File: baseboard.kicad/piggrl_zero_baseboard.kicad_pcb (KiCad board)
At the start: 2 copper layers, 101 x 43.9 mm, 61 parts, among them P1 PowerBoost 500c, P2 I2C, P3 USB_A, P4 Serial, Q1 IRF7309IPBF, Q4 MMBT2222, SW1 SW_PUSH, U1 gpio-header_zero, U2 2.2_tft_ili9340, U3 Regulator_LP2980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

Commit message: added more 3d models
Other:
- board text added: "2016-03-13"
- board text removed: "2016-03-05"

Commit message: added a nice 8bit-ish logo to the front silkscreen :-)
... that will be covered by the screen :'-(
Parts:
- added G***: LOGO, components:Logo, F.Cu at (167.5, 133.1)
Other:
- board text added: "Gnd Tx Rx"
- board text removed: "RX TX Gnd"

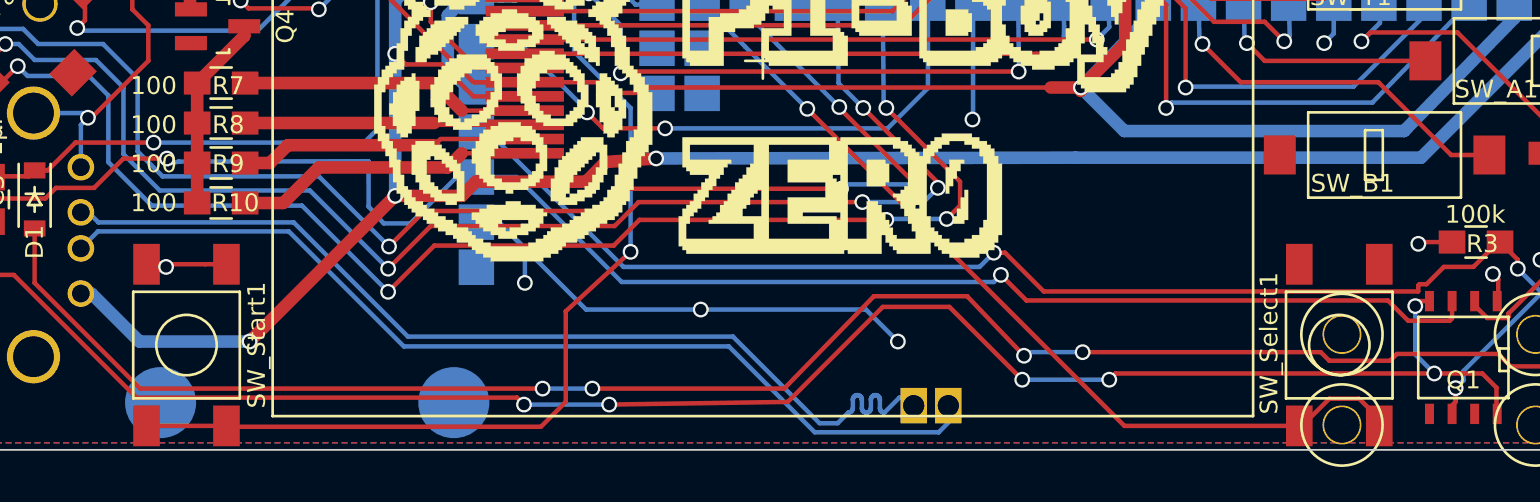
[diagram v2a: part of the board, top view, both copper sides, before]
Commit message: fixed start/select button footprint
commonly those push buttons pair their four pins the other way...
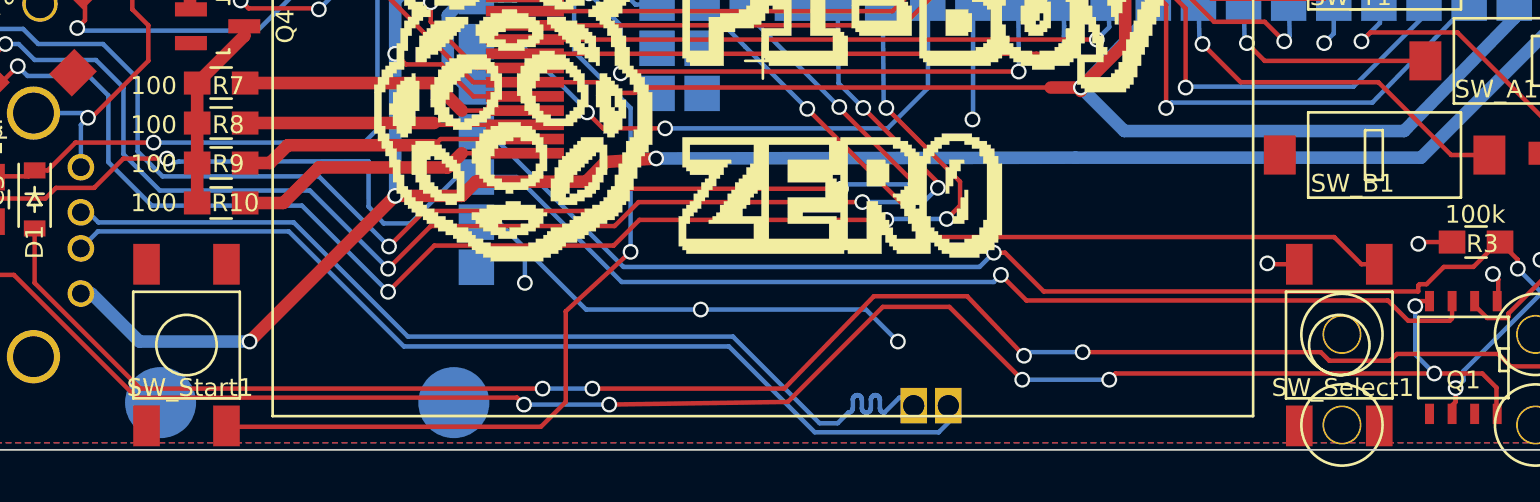
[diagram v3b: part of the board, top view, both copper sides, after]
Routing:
- net /btn_8: track 49.6 -> 44.2 mm
- net /btn_7: track 58.7 -> 54.3 mm
- net GND: track 179.8 -> 177.1 mm
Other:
- board text added: "2016-04-02"
- board text removed: "2016-03-13"
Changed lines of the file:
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@@
 (kicad_pcb (version 4) (host pcbnew 4.0.1+dfsg1-stable)
   (general
-    (links 0)
-    (no_connects 4)
-    (area 116.949999 108.949999 218.050001 152.950001)
+    (links 138)
+    (no_connects 6)
+    (area 113.016999 90.926522 234 163.200001)
     (thickness 1.6)
     (drawings 29)
-    (tracks 839)
+    (tracks 831)
     (zones 0)
     (modules 62)
@@
     (uvia_drill 0.127)
   )
-  (module switches:smd_push_button (layer F.Cu)
-    (at 199.95 147)
-    (fp_text reference SW_Select1 (at -3.95 -0.1 90) (layer F.SilkS)
-      (effects (font (size 1 1) (thickness 0.15)))
-    )
-    (fp_text value SW_PUSH (at 0 -1.3) (layer F.Fab)
-      (effects (font (size 1 1) (thickness 0.15)))
-    )
-    (fp_line (start -3 -3) (end 3 -3) (layer F.SilkS) (width 0.15))
-    (fp_line (start 3 -3) (end 3 3) (layer F.SilkS) (width 0.15))
-    (fp_line (start 3 3) (end -3 3) (layer F.SilkS) (width 0.15))
-    (fp_line (start -3 3) (end -3 -3) (layer F.SilkS) (width 0.15))
-    (fp_circle (center 0 0) (end 0 -1.7) (layer F.SilkS) (width 0.15))
-    (pad 1 smd rect (at -2.25 -4.55) (size 1.5 2.3) (layers F.Cu F.Paste F.Mask)
-      (net 4 GND))
-    (pad 1 smd rect (at 2.25 -4.55) (size 1.5 2.3) (layers F.Cu F.Paste F.Mask)
-      (net 4 GND))
-    (pad 2 smd rect (at -2.25 4.55) (size 1.5 2.3) (layers F.Cu F.Paste F.Mask)
-      (net 53 /btn_8))
-    (pad 2 smd rect (at 2.25 4.55) (size 1.5 2.3) (layers F.Cu F.Paste F.Mask)
-      (net 53 /btn_8))
-  )
   (module Connect:1pin (layer F.Cu)
     (at 211 151.5)
@@
     (pad "" thru_hole circle (at 1.5 0 90) (size 1.5 1.5) (drill 1.1) (layers *.Cu *.Mask B.SilkS))
   )
-  (module switches:smd_push_button (layer F.Cu)
-    (at 135.05 147)
-    (fp_text reference SW_Start1 (at 3.95 0 90) (layer F.SilkS)
-      (effects (font (size 1 1) (thickness 0.15)))
-    )
-    (fp_text value SW_PUSH (at 0 -1.3) (layer F.Fab)
-      (effects (font (size 1 1) (thickness 0.15)))
-    )
-    (fp_line (start -3 -3) (end 3 -3) (layer F.SilkS) (width 0.15))
-    (fp_line (start 3 -3) (end 3 3) (layer F.SilkS) (width 0.15))
-    (fp_line (start 3 3) (end -3 3) (layer F.SilkS) (width 0.15))
-    (fp_line (start -3 3) (end -3 -3) (layer F.SilkS) (width 0.15))
-    (fp_circle (center 0 0) (end 0 -1.7) (layer F.SilkS) (width 0.15))
-    (pad 1 smd rect (at -2.25 -4.55) (size 1.5 2.3) (layers F.Cu F.Paste F.Mask)
-      (net 4 GND))
-    (pad 1 smd rect (at 2.25 -4.55) (size 1.5 2.3) (layers F.Cu F.Paste F.Mask)
-      (net 4 GND))
-    (pad 2 smd rect (at -2.25 4.55) (size 1.5 2.3) (layers F.Cu F.Paste F.Mask)
-      (net 54 /btn_7))
-    (pad 2 smd rect (at 2.25 4.55) (size 1.5 2.3) (layers F.Cu F.Paste F.Mask)
-      (net 54 /btn_7))
-  )
   (module components:audio_smd_SJ-3523-SMT-TR (layer B.Cu)
     (at 116.3 127.8)
@@
       (xy -1.778 -6.688666)) (layer F.SilkS) (width 0.01))
   )
+  (module switches:smd_push_button (layer F.Cu)
+    (at 135.05 147)
+    (fp_text reference SW_Start1 (at 0.2 2.4) (layer F.SilkS)
+      (effects (font (size 1 1) (thickness 0.15)))
+    )
+    (fp_text value SW_PUSH (at 0 -1.3) (layer F.Fab)
+      (effects (font (size 1 1) (thickness 0.15)))
+    )
+    (fp_line (start -3 -3) (end 3 -3) (layer F.SilkS) (width 0.15))
+    (fp_line (start 3 -3) (end 3 3) (layer F.SilkS) (width 0.15))
+    (fp_line (start 3 3) (end -3 3) (layer F.SilkS) (width 0.15))
+    (fp_line (start -3 3) (end -3 -3) (layer F.SilkS) (width 0.15))
+    (fp_circle (center 0 0) (end 0 -1.7) (layer F.SilkS) (width 0.15))
+    (pad 1 smd rect (at -2.25 -4.55) (size 1.5 2.3) (layers F.Cu F.Paste F.Mask)
+      (net 4 GND))
+    (pad 2 smd rect (at 2.25 -4.55) (size 1.5 2.3) (layers F.Cu F.Paste F.Mask)
+      (net 54 /btn_7))
+    (pad 1 smd rect (at -2.25 4.55) (size 1.5 2.3) (layers F.Cu F.Paste F.Mask)
+      (net 4 GND))
+    (pad 2 smd rect (at 2.25 4.55) (size 1.5 2.3) (layers F.Cu F.Paste F.Mask)
+      (net 54 /btn_7))
+  )
+  (module switches:smd_push_button (layer F.Cu)
+    (at 199.95 147)
+    (fp_text reference SW_Select1 (at 0.2 2.4) (layer F.SilkS)
+      (effects (font (size 1 1) (thickness 0.15)))
+    )
+    (fp_text value SW_PUSH (at 0 -1.3) (layer F.Fab)
+      (effects (font (size 1 1) (thickness 0.15)))
+    )
+    (fp_line (start -3 -3) (end 3 -3) (layer F.SilkS) (width 0.15))
+    (fp_line (start 3 -3) (end 3 3) (layer F.SilkS) (width 0.15))
+    (fp_line (start 3 3) (end -3 3) (layer F.SilkS) (width 0.15))
+    (fp_line (start -3 3) (end -3 -3) (layer F.SilkS) (width 0.15))
+    (fp_circle (center 0 0) (end 0 -1.7) (layer F.SilkS) (width 0.15))
+    (pad 1 smd rect (at -2.25 -4.55) (size 1.5 2.3) (layers F.Cu F.Paste F.Mask)
+      (net 4 GND))
+    (pad 2 smd rect (at 2.25 -4.55) (size 1.5 2.3) (layers F.Cu F.Paste F.Mask)
+      (net 53 /btn_8))
+    (pad 1 smd rect (at -2.25 4.55) (size 1.5 2.3) (layers F.Cu F.Paste F.Mask)
+      (net 4 GND))
+    (pad 2 smd rect (at 2.25 4.55) (size 1.5 2.3) (layers F.Cu F.Paste F.Mask)
+      (net 53 /btn_8))
+  )
   (dimension 37.6 (width 0.3) (layer Eco2.User)
     (gr_text "37.600 mm" (at 195.9 157.15) (layer Eco2.User)
@@
     (arrow2b (pts (xy 214.7 155.8) (xy 213.573496 156.386421)))
   )
-  (gr_text 2016-03-13 (at 171.1 120.5) (layer B.SilkS)
+  (gr_text 2016-04-02 (at 171.1 120.5) (layer B.SilkS)
     (effects (font (size 1.5 1.5) (thickness 0.3)) (justify mirror))
   )
@@
   (segment (start 155.7 119.1) (end 155.7 117.85) (width 0.254) (layer B.Cu) (net 3))
   (segment (start 155.7 117.85) (end 154.55 116.7) (width 0.254) (layer B.Cu) (net 3))
-  (segment (start 133.9 142.6) (end 133.7 142.4) (width 0.254) (layer F.Cu) (net 4))
-  (segment (start 133.7 142.4) (end 132.9 142.4) (width 0.254) (layer F.Cu) (net 4))
-  (segment (start 132.9 142.4) (end 132.85 142.45) (width 0.254) (layer F.Cu) (net 4))
-  (segment (start 132.85 142.45) (end 132.8 142.45) (width 0.254) (layer F.Cu) (net 4))
-  (segment (start 136.1 142.45) (end 137.3 142.45) (width 0.254) (layer F.Cu) (net 4))
+  (segment (start 197.7 142.45) (end 195.95 142.45) (width 0.254) (layer F.Cu) (net 4))
+  (segment (start 195.95 142.45) (end 195.9 142.4) (width 0.254) (layer F.Cu) (net 4))
+  (via (at 195.9 142.4) (size 0.889) (drill 0.635) (layers F.Cu B.Cu) (net 4))
   (segment (start 208.84 144.525) (end 208.9 144.525) (width 0.254) (layer F.Cu) (net 4))
   (segment (start 208.9 144.525) (end 208.9 143.3) (width 0.254) (layer F.Cu) (net 4))
   (segment (start 208.9 143.3) (end 208.6 143) (width 0.254) (layer F.Cu) (net 4))
-  (segment (start 136.1 142.45) (end 134.05 142.45) (width 0.254) (layer F.Cu) (net 4))
-  (segment (start 134.05 142.45) (end 133.9 142.6) (width 0.254) (layer F.Cu) (net 4))
   (segment (start 199.64 127.8) (end 199.64 129.46) (width 0.254) (layer B.Cu) (net 4))
   (segment (start 199.64 129.46) (end 199.1 130) (width 0.254) (layer B.Cu) (net 4))
@@
   (segment (start 157.544 145) (end 164 145) (width 0.254) (layer B.Cu) (net 4))
   (via (at 164 145) (size 0.889) (drill 0.635) (layers F.Cu B.Cu) (net 4))
-  (via (at 133.9 142.6) (size 0.889) (drill 0.635) (layers F.Cu B.Cu) (net 4))
   (segment (start 142.5 128.1) (end 144.2 126.4) (width 0.254) (layer B.Cu) (net 4))
   (segment (start 144.2 126.4) (end 144.2 125.1) (width 0.254) (layer B.Cu) (net 4))
@@
   (segment (start 157.2 110.7) (end 157.5 110.4) (width 0.254) (layer B.Cu) (net 4))
   (segment (start 149.9 112.1) (end 149.35 112.1) (width 0.254) (layer B.Cu) (net 4))
+  (segment (start 197.7 151.55) (end 197.858118 151.55) (width 0.254) (layer F.Cu) (net 4))
   (segment (start 120.7 132.1) (end 120.7 129.7) (width 0.254) (layer B.Cu) (net 5))
   (segment (start 140.5 110.1) (end 141.55 110.1) (width 0.254) (layer B.Cu) (net 5))
@@
   (via (at 157.7 127.2) (size 0.889) (drill 0.635) (layers F.Cu B.Cu) (net 52))
   (segment (start 157.5 127.4) (end 157.7 127.2) (width 0.254) (layer F.Cu) (net 52))
-  (segment (start 197.7 151.55) (end 197.858118 151.55) (width 0.254) (layer F.Cu) (net 53))
-  (segment (start 197.858118 151.55) (end 199.389119 150.018999) (width 0.254) (layer F.Cu) (net 53))
-  (segment (start 199.389119 150.018999) (end 201.068999 150.018999) (width 0.254) (layer F.Cu) (net 53))
-  (segment (start 201.068999 150.018999) (end 202.2 151.15) (width 0.254) (layer F.Cu) (net 53))
-  (segment (start 202.2 151.15) (end 202.2 151.55) (width 0.254) (layer F.Cu) (net 53))
-  (segment (start 170 133.7) (end 187.85 151.55) (width 0.254) (layer F.Cu) (net 53))
-  (segment (start 187.85 151.55) (end 197.858118 151.55) (width 0.254) (layer F.Cu) (net 53))
-  (segment (start 164.09 127.74) (end 166.5 130.2) (width 0.254) (layer B.Cu) (net 53) (status 10))
+  (segment (start 170 133.7) (end 177.218999 140.918999) (width 0.254) (layer F.Cu) (net 53))
+  (segment (start 177.218999 140.918999) (end 199.664999 140.918999) (width 0.254) (layer F.Cu) (net 53))
+  (segment (start 199.664999 140.918999) (end 201.196 142.45) (width 0.254) (layer F.Cu) (net 53))
+  (segment (start 201.196 142.45) (end 202.2 142.45) (width 0.254) (layer F.Cu) (net 53))
   (via (at 170 133.7) (size 0.889) (drill 0.635) (layers F.Cu B.Cu) (net 53))
+  (segment (start 164.09 127.74) (end 166.5 130.2) (width 0.254) (layer B.Cu) (net 53) (status 10))
   (segment (start 166.5 130.2) (end 170 133.7) (width 0.254) (layer B.Cu) (net 53))
-  (segment (start 132.8 151.55) (end 137.15 151.55) (width 0.254) (layer F.Cu) (net 54))
   (segment (start 137.15 151.55) (end 137.2 151.6) (width 0.254) (layer F.Cu) (net 54))
   (segment (start 137.2 151.6) (end 137.25 151.55) (width 0.254) (layer F.Cu) (net 54))
